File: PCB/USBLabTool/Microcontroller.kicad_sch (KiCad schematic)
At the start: 14 parts, among them U12 STM32H562VGTx, Y1 32.768kHz

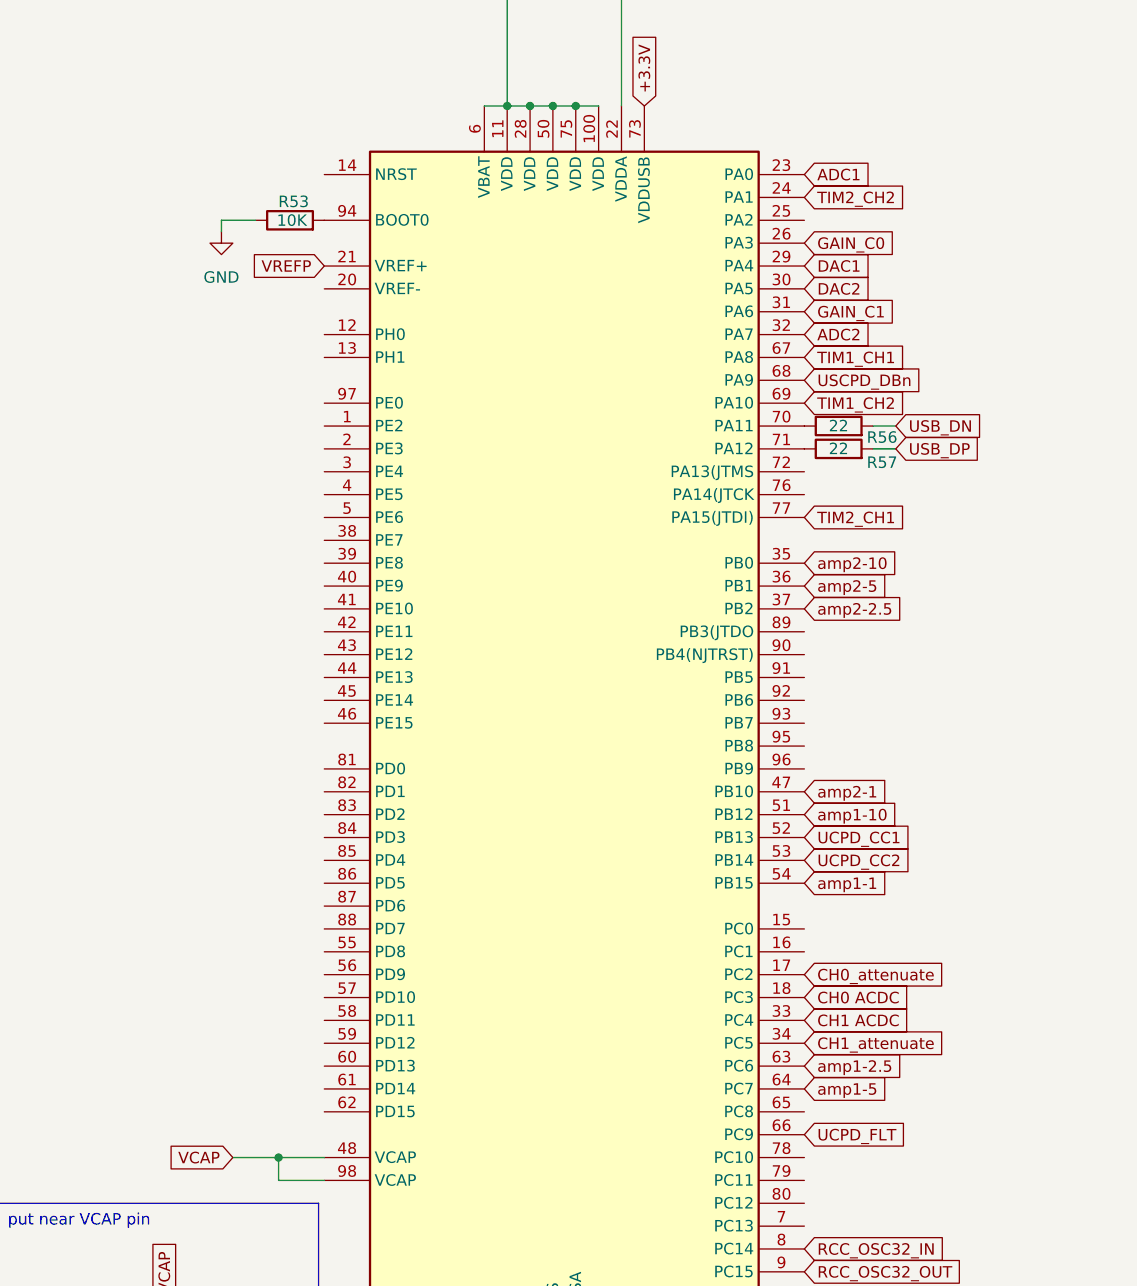
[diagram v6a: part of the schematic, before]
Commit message: modify MCU and name tags
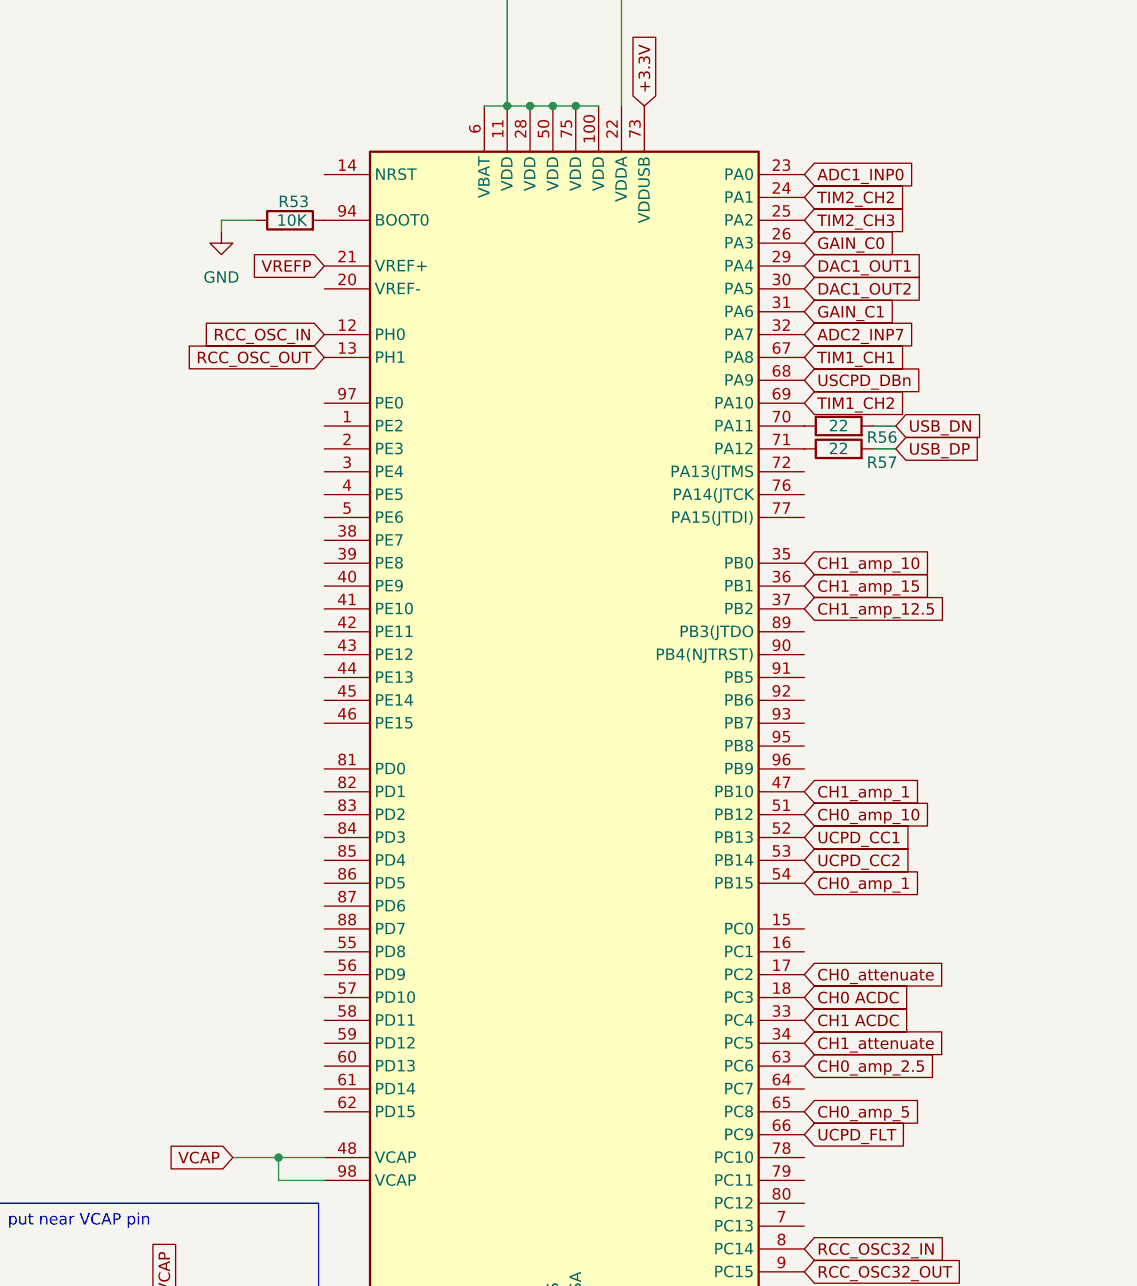
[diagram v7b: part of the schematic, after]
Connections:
- net RCC_OSC_IN: now also U12.12 (PH0)
- net RCC_OSC_OUT: now also U12.13 (PH1)
- net TIM2_CH3: now reaches U12.25 (PA2)
- net CH0_amp_5: now reaches U12.65 (PC8)
- net ADC1 renamed ADC1_INP0
- net ADC2 renamed ADC2_INP7
- net DAC1 renamed DAC1_OUT1
- net DAC2 renamed DAC1_OUT2
- net TIM2_CH1: no longer names the net of U12.77 (PA15(JTDI))
- net amp1-1 renamed CH0_amp_1
- net amp1-10 renamed CH0_amp_10
- net amp1-2.5 renamed CH0_amp_2.5
- net amp1-5: no longer names the net of U12.64 (PC7)
- net amp2-1 renamed CH1_amp_1
- net amp2-10 renamed CH1_amp_10
- net amp2-2.5 renamed CH1_amp_12.5
- net amp2-5 renamed CH1_amp_15

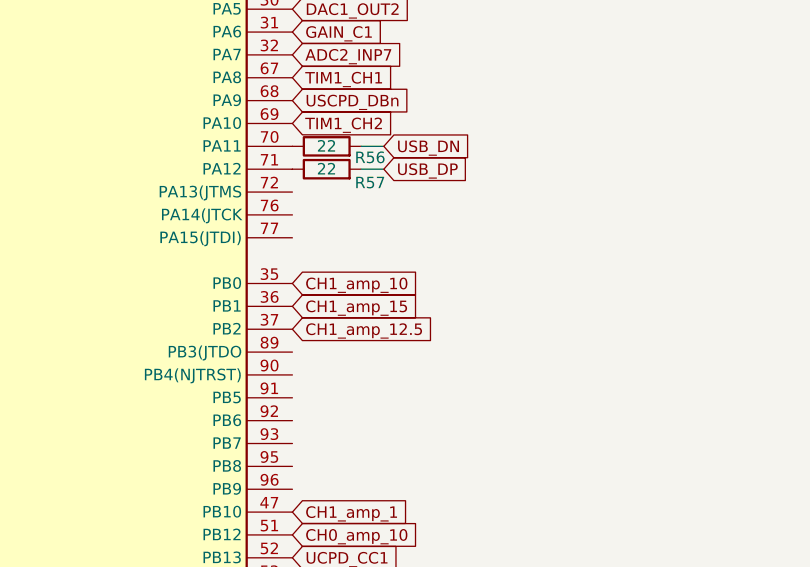
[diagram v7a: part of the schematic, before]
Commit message: add usb protection
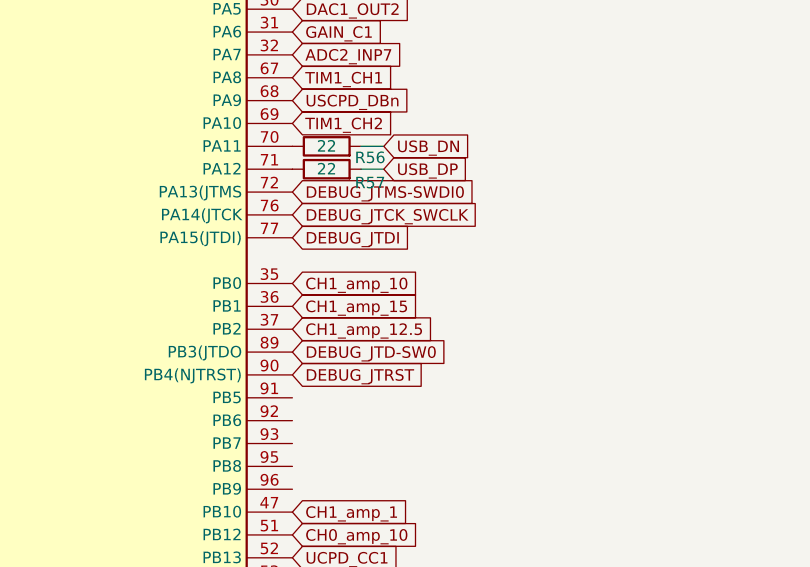
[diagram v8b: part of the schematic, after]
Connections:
- net DEBUG_JTMS-SWDI0: now reaches U12.72 (PA13(JTMS)
- net DEBUG_JTCK_SWCLK: now reaches U12.76 (PA14(JTCK)
- net DEBUG_JTDI: now reaches U12.77 (PA15(JTDI))
- net DEBUG_JTD-SW0: now reaches U12.89 (PB3(JTDO)
- net DEBUG_JTRST: now reaches U12.90 (PB4(NJTRST))
